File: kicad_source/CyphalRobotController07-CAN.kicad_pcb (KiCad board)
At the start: 2 copper layers, 140 x 70 mm, 185 parts, among them J1 BM04B-SRSS-TB, J10 x, J11 PowerPole, J12 Conn_01x02, J13 Conn_01x02, J14 Conn_01x02, J15 PinHeader_1x04, J16 PinHeader_1x04, J17 PinHeader_1x05, J18 Conn_01x02, J19 S6B-XH-A, J2 RASPBERRYPI_PICO, J20 S6B-XH-A, J3 BM04B-SRSS-TB, J4 B3B-PH-SM4-TB, J5 BM04B-GHS-TBT, J6 BM04B-GHS-TBT, J7 x, J8 x, J9 x, Q1 2N7002, Q2 IPD90P03P4L- 04, SW1 PTS636 SM43 SMTR LFS, U1 24LC64-I/SN, U10 ADS1015IDGS, U11 OPA2374AIDCN, U12 INA226, U13 IFX91041EFJ, U14 ITS4200S-ME-P, U15 ITS4200S-ME-P, U16 BNO085, U17 SN74LVC2T45DCUR, U18 SN74LVC2T45DCUR, U2 MCP2515-I/SO, U3 SN65HVD232, U4 74xx08, U5 IFX007T, U6 IFX007T, U7 IFX007T, U8 IFX007T, U9 OPA2374AIDCN, Y1 RH100-16.000-16-3030-EXT-TR, Y2 DNI

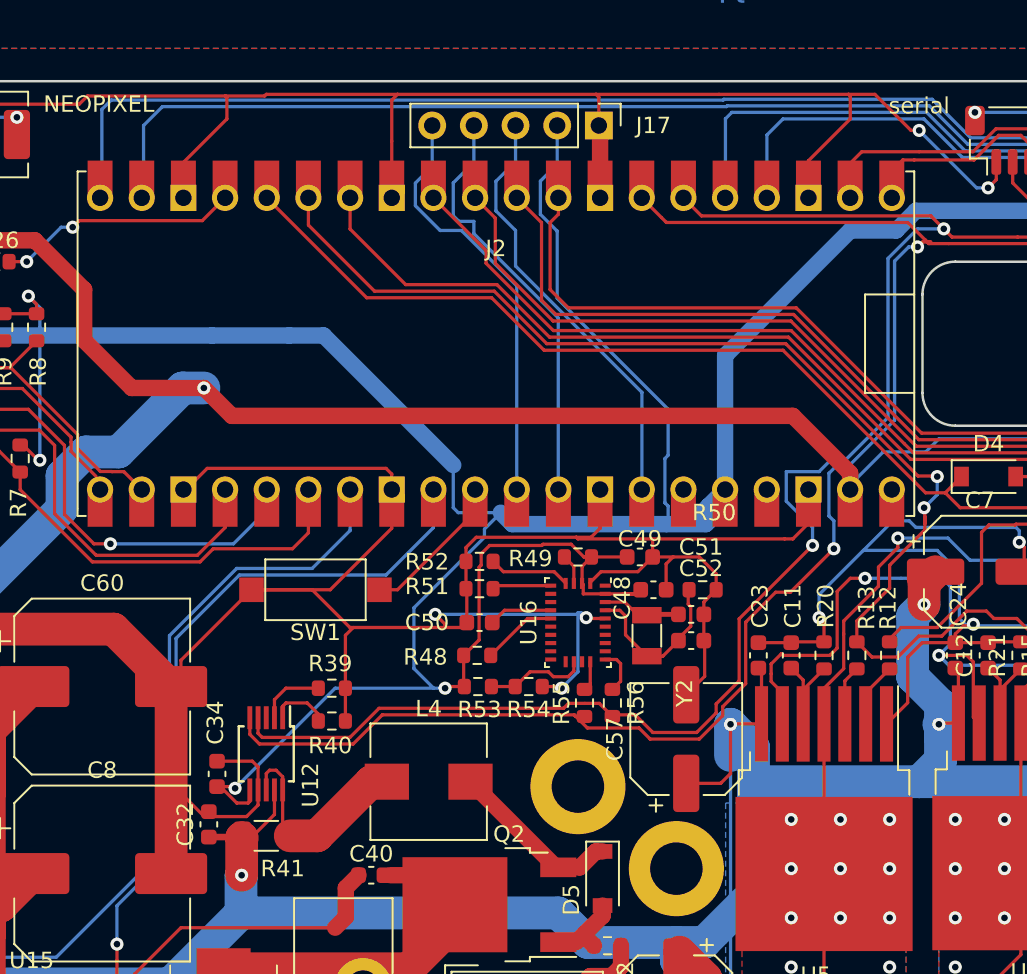
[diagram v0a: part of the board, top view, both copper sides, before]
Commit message: checked supply voltage of parts
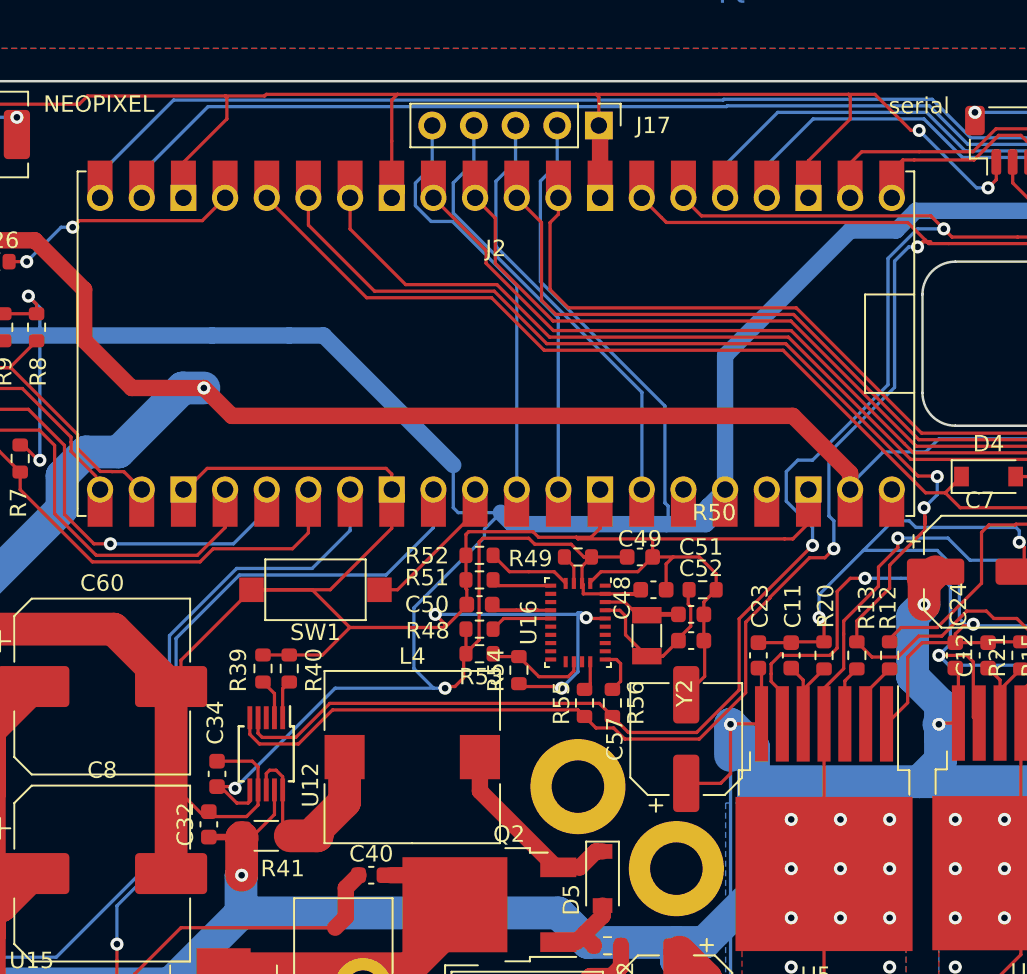
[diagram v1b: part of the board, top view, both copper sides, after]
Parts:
- L4: footprint Inductor_SMD:L_Wuerth_HCI-7050 -> Inductor_SMD:L_Wuerth_HCM-1052
- Q2: value IPD90P03P4L- 04 -> IPD90P04P4L- 04
- moved R39 4.37 mm to (101.8, 91.8), turned to 90 degrees
- moved R40 4.12 mm to (103.4, 91.8), turned to 90 degrees
- moved R53 2.00 mm to (115.0, 90.9)
- moved L4 1.80 mm to (110.9, 97.2)
- moved R48 1.61 mm to (115.0, 89.4)
- moved R54 1.17 mm to (117.4, 91.9), turned to -90 degrees
- moved C50 1.10 mm to (115.0, 87.9)
- moved R51 0.53 mm to (115.0, 86.4)
- moved R52 0.37 mm to (115.0, 84.9)
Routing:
- net /BNO085/CAP: track 3.87 -> 6.13 mm
- net /QUAD1_U: track 126.0 -> 123.8 mm
- net GND: track 1155.7 -> 1157.5 mm
- net /QUAD3_U: track 87.0 -> 85.3 mm
- net /QUAD0_U: track 122.0 -> 120.4 mm
- net Net-(R39-Pad1): track 4.06 -> 2.46 mm
- net +3.3V: track 356.9 -> 358.3 mm
- net /VoltageRegulator/+BATT_I: track 10.6 -> 12.0 mm
- net Net-(R40-Pad1): track 3.66 -> 2.34 mm
- net I2C_SDA: track 134.2 -> 132.9 mm
- net /QUAD2_U: track 83.1 -> 82.0 mm
- net I2C_SCL: track 133.5 -> 132.6 mm
- net /BNO085/CLKSEL0: track 4.59 -> 3.78 mm
- net /ANALOG_INPUT1: track 25.8 -> 25.3 mm

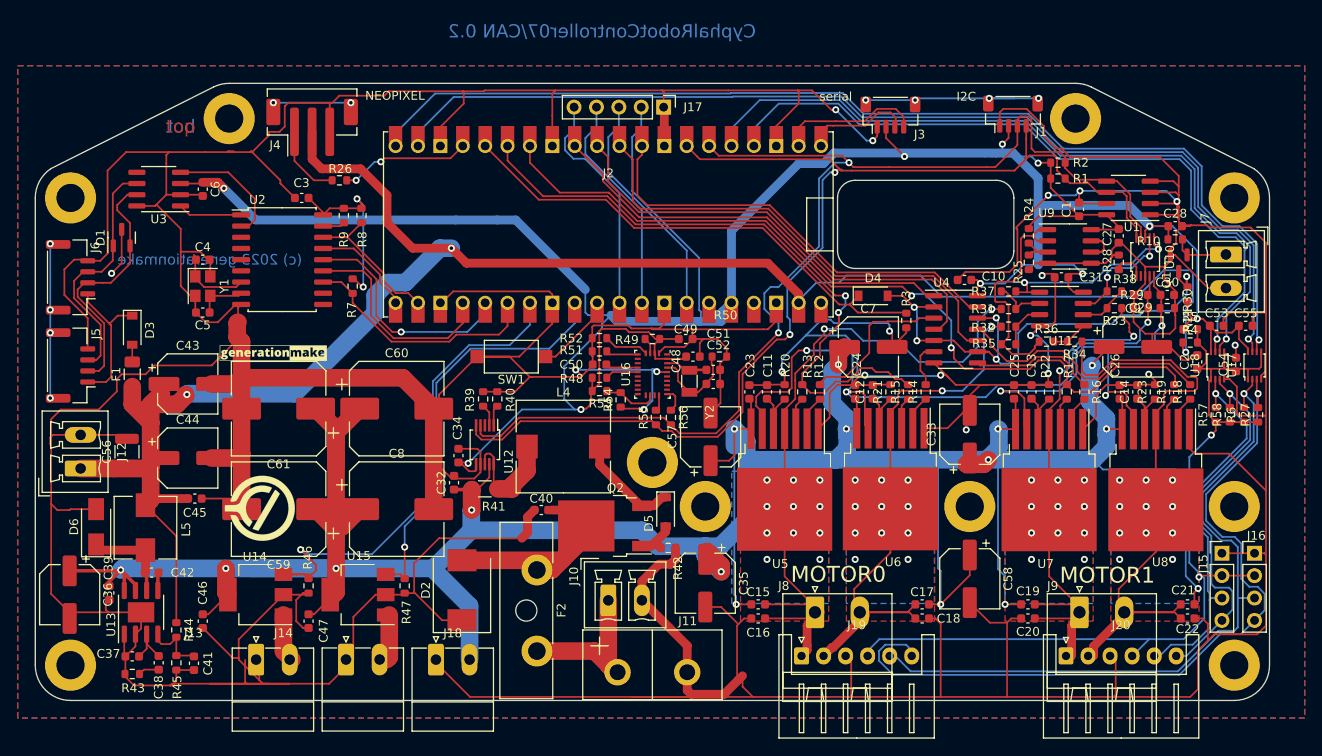
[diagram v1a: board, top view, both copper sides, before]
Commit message: replaced INA226 by INA232 to support up to 40V
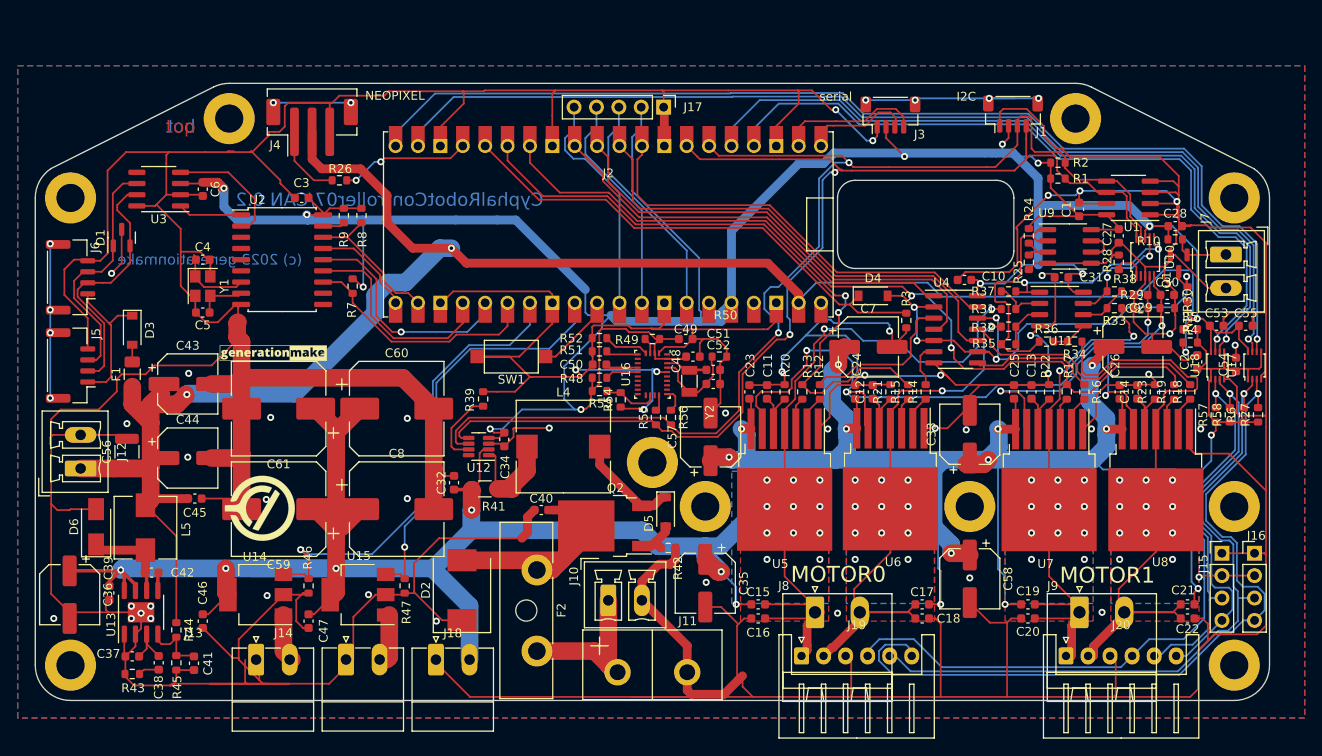
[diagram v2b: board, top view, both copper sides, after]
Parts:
- removed R40: 0R, Resistor_SMD:R_0603_1608Metric
- U12: value INA226 -> INA232AIDDFR; footprint Package_SO:MSOP-10_3x3mm_P0.5mm -> Package_TO_SOT_SMD:SOT-23-8
- moved C34 5.51 mm to (104.2, 96.4), turned to -90 degrees
- moved U12 0.73 mm to (101.3, 97.2), turned to 180 degrees
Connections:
- U12 pad 1: Net-(R40-Pad1) -> /VoltageRegulator/+BATT_R
- U12 pad 2: Net-(R39-Pad1) -> +BATT
- U12 pad 3: unconnected-(U12-Pad3) -> GND
- U12 pad 4: I2C_SDA -> +3.3V
- U12 pad 6: +3.3V -> I2C_SDA
- U12 pad 7: GND -> Net-(R39-Pad1)
- U12 pad 8: /VoltageRegulator/+BATT_R -> unconnected-(U12-Pad8)
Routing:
- net GND: track 1157.5 -> 1143.8 mm, vias 19 -> 46
- net +BATT: track 392.6 -> 380.5 mm, vias 16 -> 18
- net Net-(R39-Pad1): track 2.46 -> 8.82 mm
- net +3.3V: track 358.3 -> 353.5 mm
- net I2C_SDA: track 132.9 -> 137.2 mm
- net OUTPUT0: track 58.5 -> 55.1 mm
- net Net-(R40-Pad1): track 2.34 -> 0.00 mm
- net I2C_SCL: track 132.6 -> 134.5 mm
- net IS12: track 75.3 -> 73.8 mm
- net QUAD0: track 79.8 -> 78.4 mm
- net /VoltageRegulator/+BATT_R: track 13.3 -> 11.9 mm
- net IS34: track 48.8 -> 47.5 mm
- net QUAD3: track 42.7 -> 41.6 mm
- net QUAD2: track 43.4 -> 42.3 mm
- net /MotorDriver/PWM4_U: track 29.9 -> 28.9 mm
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
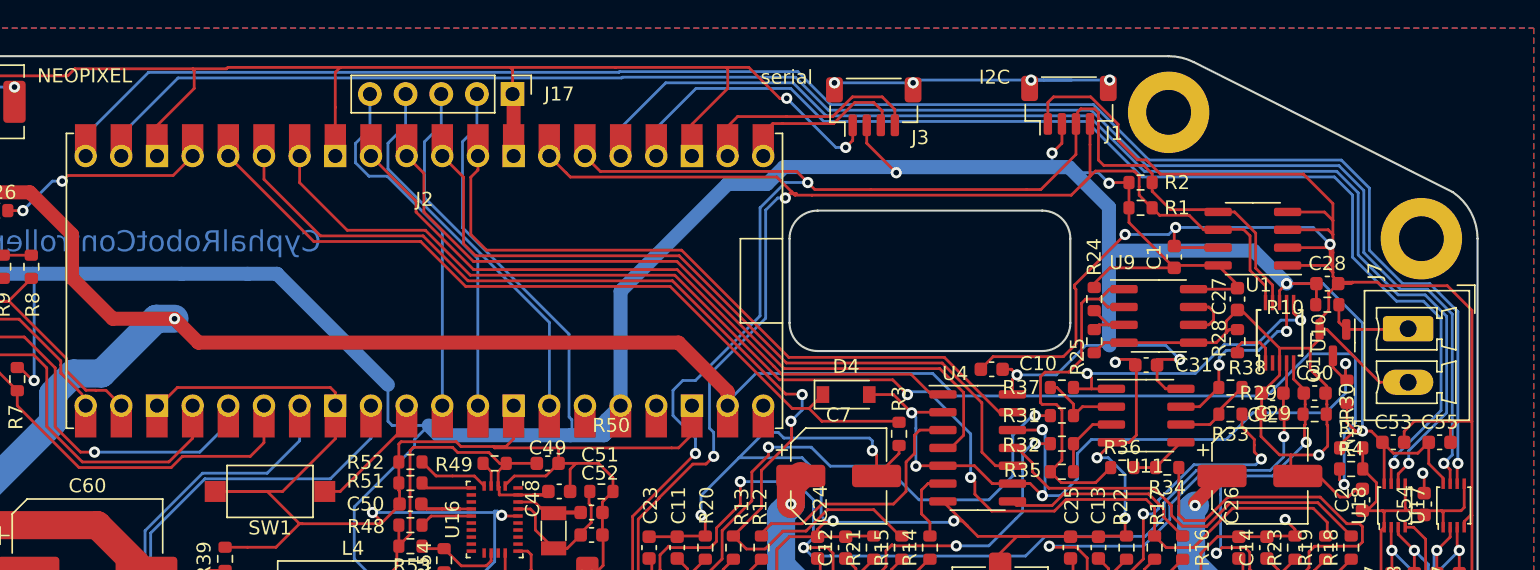
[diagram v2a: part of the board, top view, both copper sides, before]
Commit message: connected current sense output to analog in of RP2040
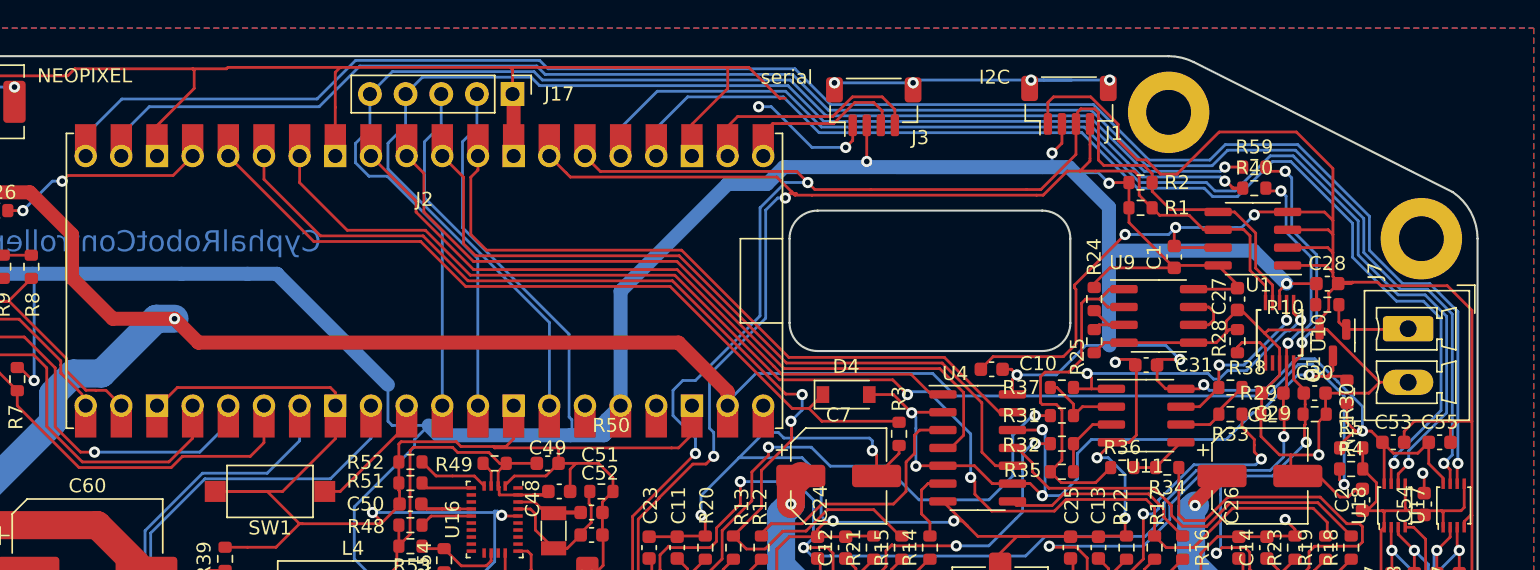
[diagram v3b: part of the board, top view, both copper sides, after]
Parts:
- added R40: 100R, Resistor_SMD:R_0603_1608Metric, F.Cu at (175.1, 65.4)
- added R59: 100R, Resistor_SMD:R_0603_1608Metric, F.Cu at (175.1, 63.9)
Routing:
- net /ANALOG_INPUT0: track 25.9 -> 92.2 mm, vias 0 -> 1
- net /ANALOG_INPUT1: track 25.3 -> 89.6 mm, vias 0 -> 1
- net IS34: track 47.5 -> 64.2 mm, vias 3 -> 5
- net IS12: track 73.8 -> 89.0 mm, vias 3 -> 5
- net +5V: track 216.2 -> 212.9 mm
- net /MotorDriver/EM_STOP_Q: track 58.7 -> 55.9 mm
- net GND: track 1143.8 -> 1145.4 mm
- net +3.3V: track 353.5 -> 355.0 mm, vias 12 -> 13
- net I2C_SCL: track 134.5 -> 133.5 mm
- net /Measurement/VS34: track 13.0 -> 12.3 mm

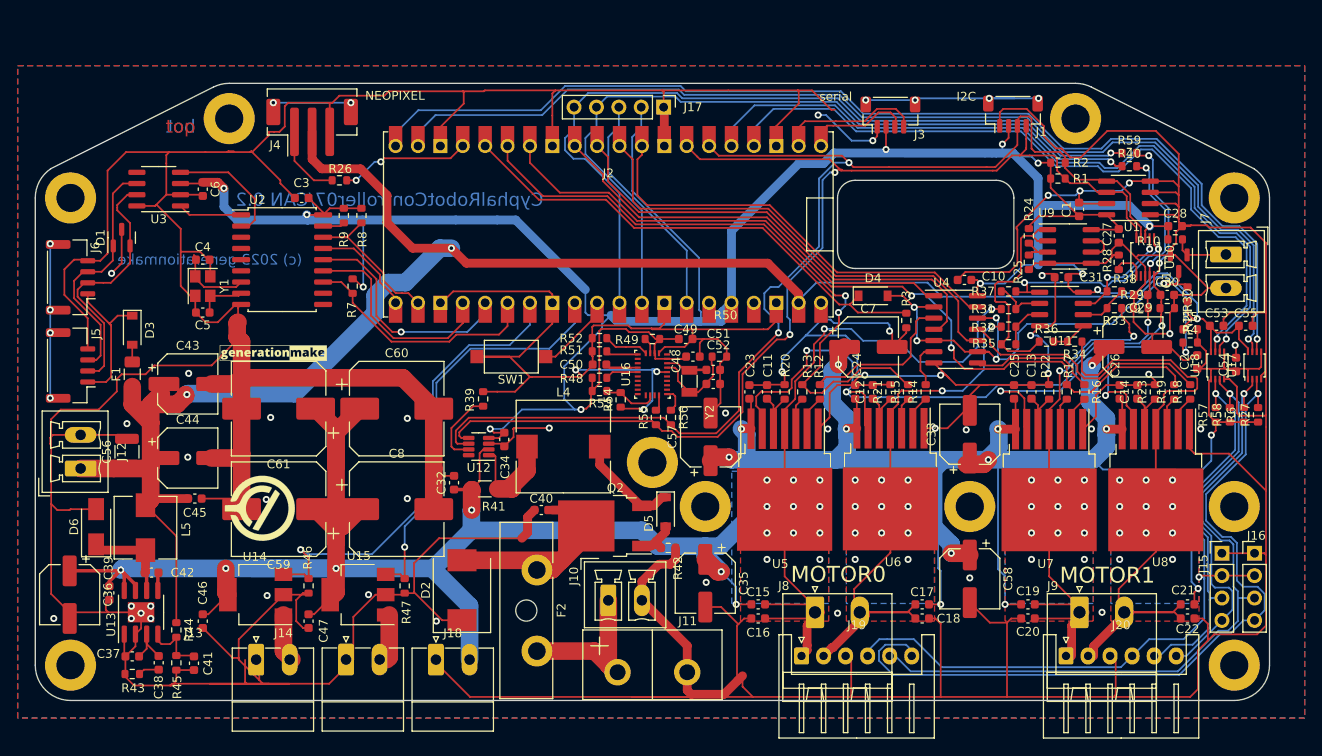
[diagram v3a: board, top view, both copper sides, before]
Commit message: fixed some drc errors
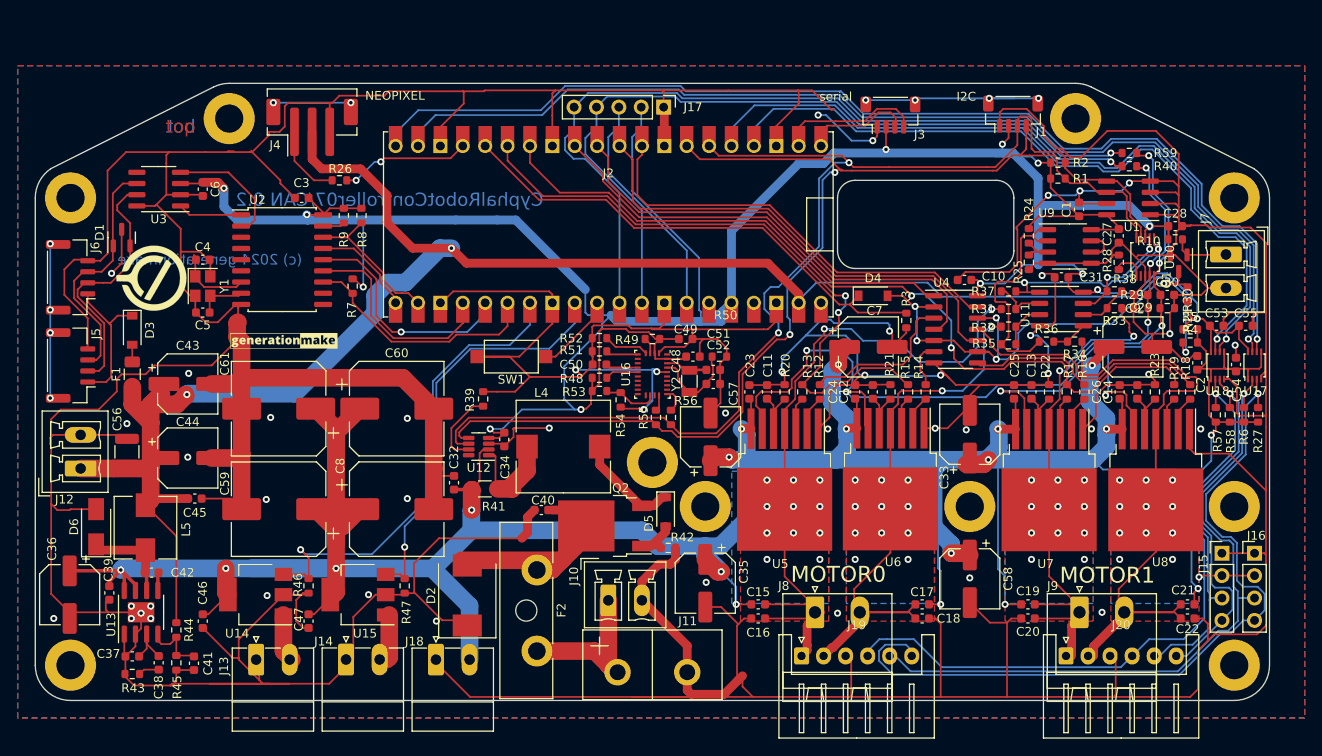
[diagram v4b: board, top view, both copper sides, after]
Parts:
- moved L2 94.2 mm to (102.9, 61.0), turned to 0 degrees
- moved L3 28.9 mm to (64.2, 78.1)
- moved L1 1.84 mm to (79.2, 87.8)
- moved D2 0.85 mm to (100.0, 114.1)
- moved C2 0.10 mm to (182.8, 87.7)
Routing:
- net +3.3V: track 355.0 -> 344.6 mm
- net GND: track 1145.4 -> 1140.8 mm
- net OUTPUT0: track 55.1 -> 53.6 mm
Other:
- board text added: "(c) 2024 generationmake"
- board text removed: "(c) 2023 generationmake"
